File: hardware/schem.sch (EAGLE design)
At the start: 8 parts

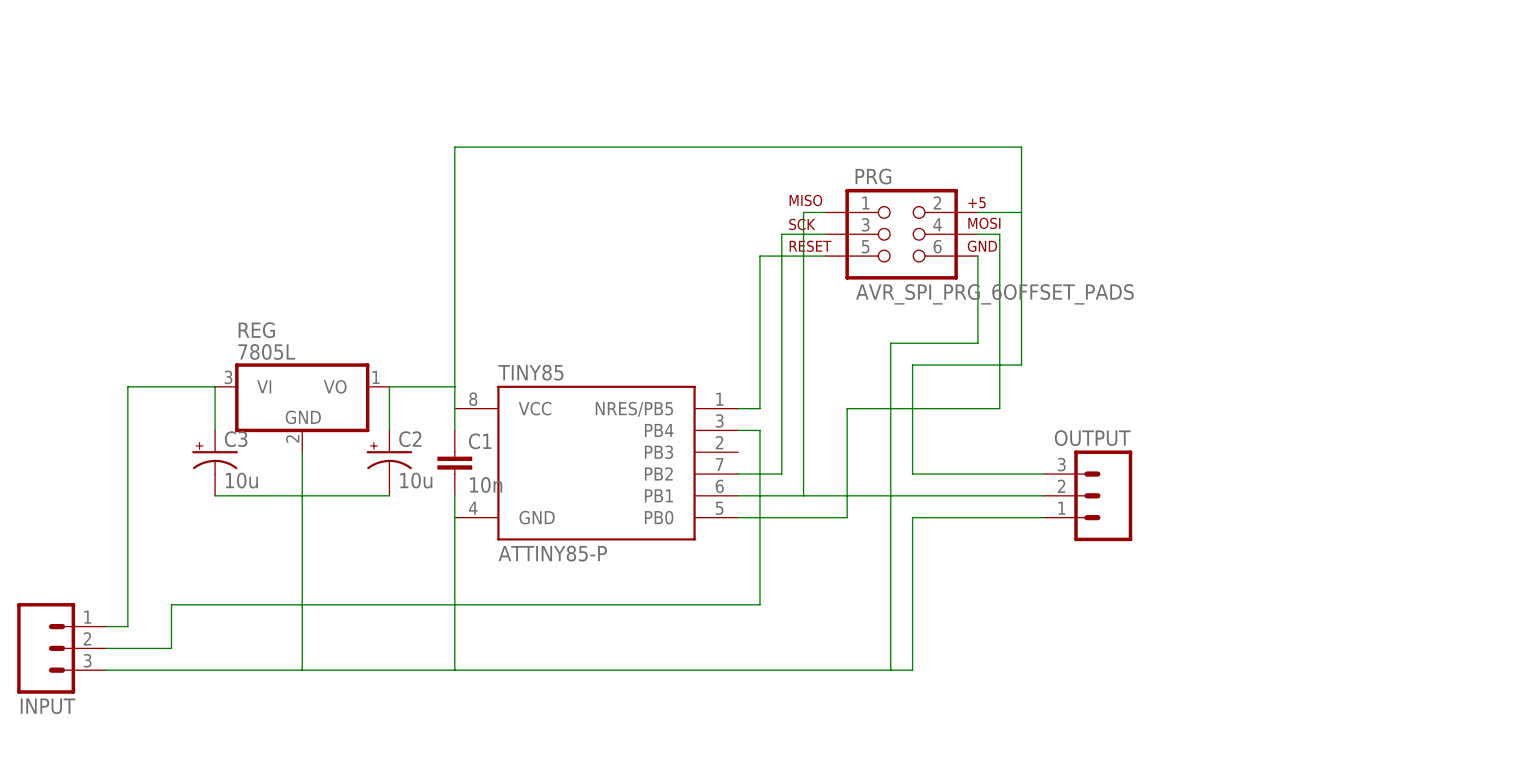
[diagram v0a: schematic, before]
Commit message: Updated Schematic to use integrated H Bridge with DC Motor
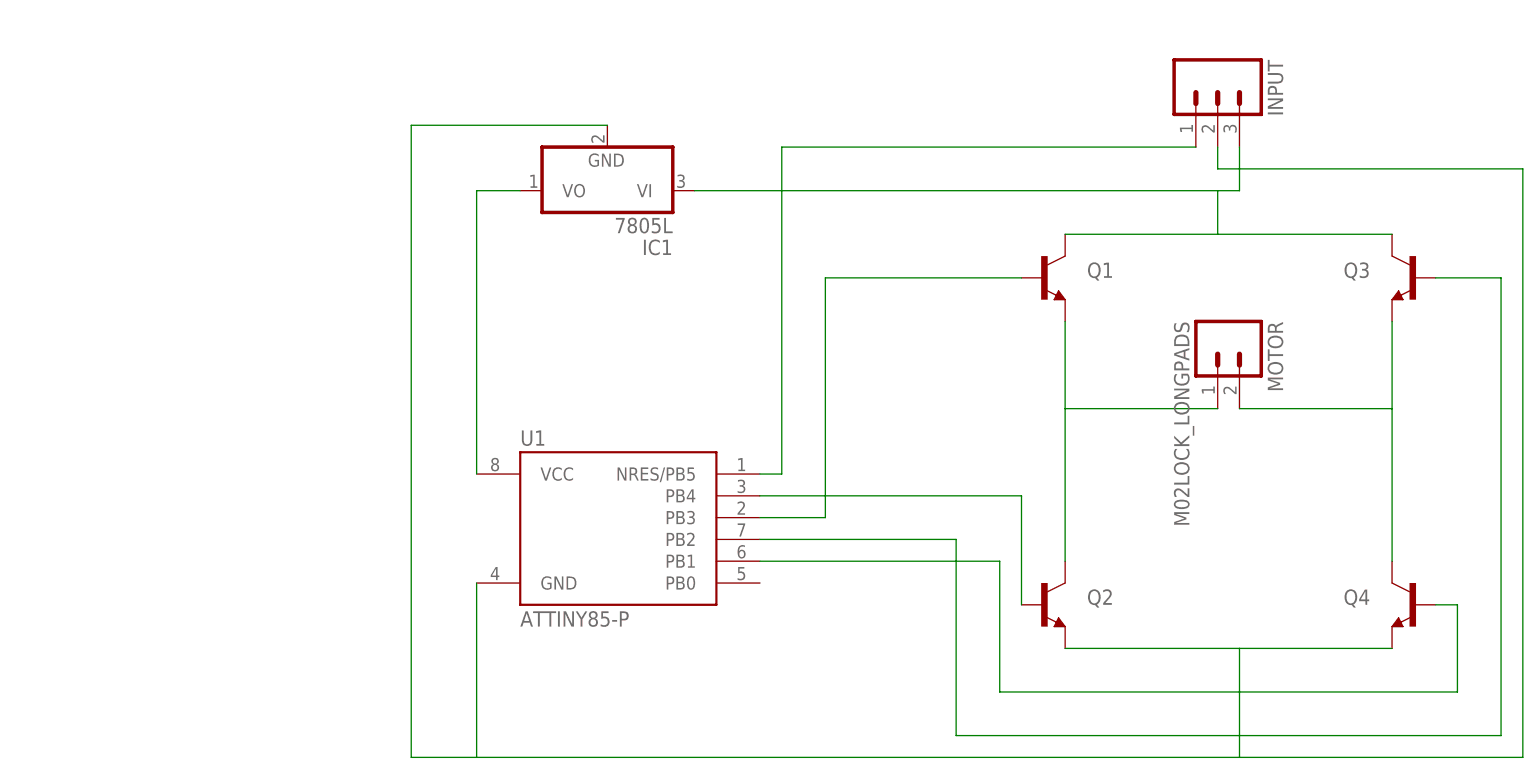
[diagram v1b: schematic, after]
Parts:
- removed C1: 10n, SparkFun-Capacitors:CAPEZ
- removed C2, C3: 10u, rcl:CPOL-USE2.5-6
- removed OUTPUT: (no value), SparkFun-Connectors:M03LOCK_LONGPADS
- removed PRG: AVR_SPI_PRG_6OFFSET_PADS, SparkFun-Connectors:AVR_SPI_PRG_6OFFSET_PADS
- removed REG: 7805L, linear:7805L
- removed TINY85: ATTINY85-P, _hhn_attiny25_45_85:ATTINY85-P
- added IC1: 7805L, linear:7805L
- added MOTOR: M02LOCK_LONGPADS, SparkFun-Connectors:M02LOCK_LONGPADS
- added Q1, Q2, Q3, Q4: (no value), SparkFun-DiscreteSemi:TRANSISTOR_NPNTO-92-AMMO
- added U1: ATTINY85-P, _hhn_attiny25_45_85:ATTINY85-P
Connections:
- new net N$1: MOTOR.1, Q1.E, Q2.C
- new net N$10: IC1.VO, U1.VCC
- net N$2: now also MOTOR.2, Q3.E, Q4.C; no longer PRG.3, TINY85.PB2
- net N$3: now also INPUT.1, U1.NRES/PB5; no longer PRG.5, TINY85.NRES/PB5
- net N$4: now also Q1.B, U1.PB3; no longer PRG.4, TINY85.PB0
- net N$5: now also IC1.VI, INPUT.3, Q1.C, Q3.C; no longer OUTPUT.2, PRG.1, TINY85.PB1
- net N$6: now also IC1.GND, Q2.E, Q4.E, U1.GND; no longer TINY85.PB4
- net N$7: now also Q2.B, U1.PB4; no longer C3.+, INPUT.1, REG.VI
- net N$8: now also Q4.B, U1.PB1; no longer C1.1, C2.+, OUTPUT.3, PRG.2, REG.VO, TINY85.VCC
- net N$9: now also Q3.B, U1.PB2; no longer C1.2, C2.-, C3.-, INPUT.3, OUTPUT.1, PRG.6, REG.GND, TINY85.GND
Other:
- moved on the sheet: INPUT

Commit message: Updated Schematic and Board to include AVR ISP Header
Changed the structure of the H Bridge as well. No longer are you able to independently control all 4 "switches". Now, you control the motor with tow pins (forward or reverse). Layout has yet to bo optimized.
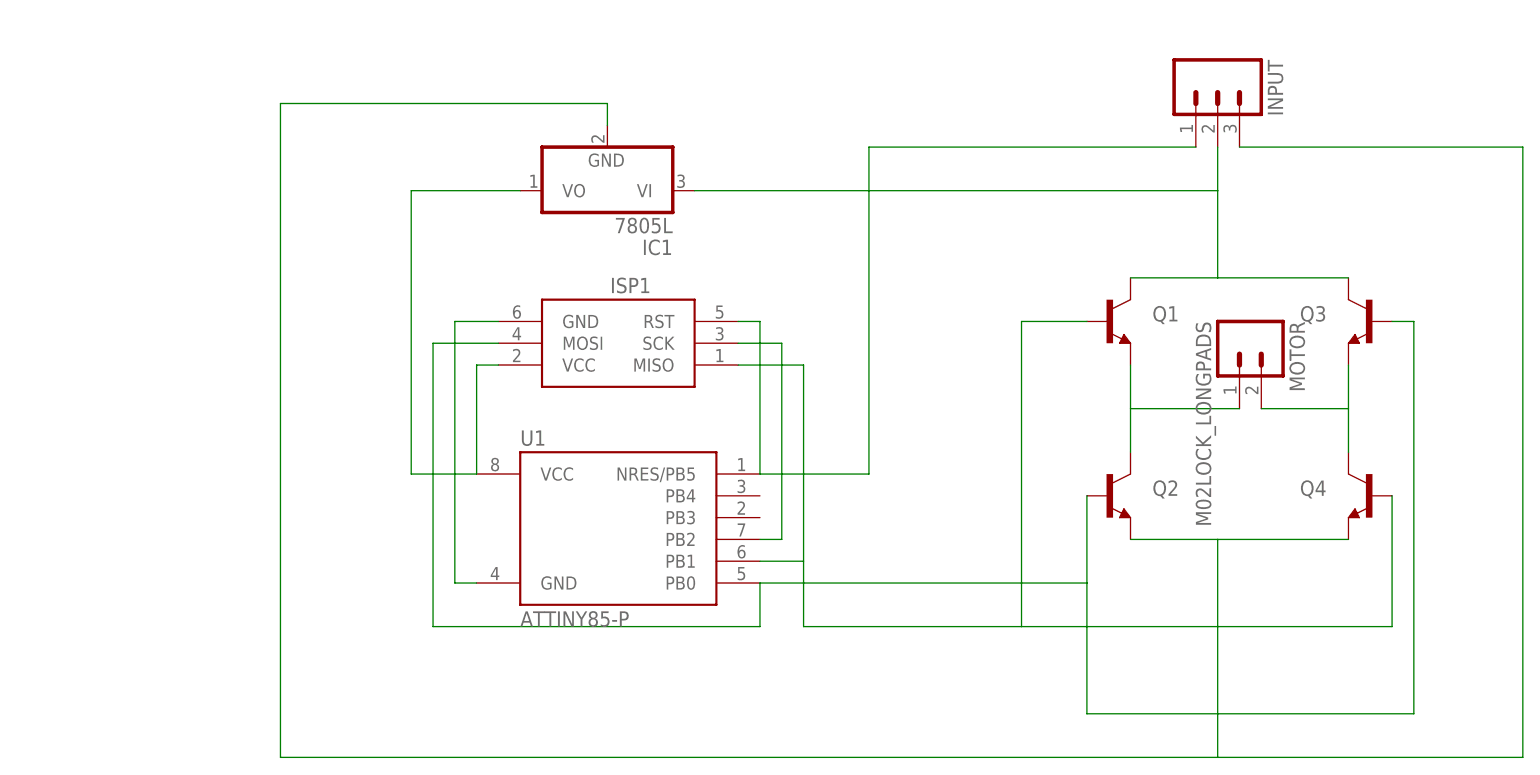
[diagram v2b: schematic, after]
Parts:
- added ISP1: AVRISP-6, adafruit:AVRISP-6
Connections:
- net N$10: now also ISP1.SCK, U1.PB2; no longer IC1.VO, U1.VCC
- net N$3: now also IC1.GND, INPUT.3, Q2.E, Q4.E; no longer INPUT.1, U1.NRES/PB5
- net N$4: now also IC1.VI, INPUT.2, Q1.C, Q3.C; no longer Q1.B, U1.PB3
- net N$5: now also ISP1.MISO, Q1.B, Q4.B, U1.PB1; no longer IC1.VI, INPUT.3, Q1.C, Q3.C
- net N$6: now also ISP1.GND; no longer IC1.GND, INPUT.2, Q2.E, Q4.E
- net N$7: now also IC1.VO, ISP1.VCC, U1.VCC; no longer Q2.B, U1.PB4
- net N$8: now also ISP1.MOSI, Q2.B, Q3.B, U1.PB0; no longer Q4.B, U1.PB1
- net N$9: now also INPUT.1, ISP1.RST, U1.NRES/PB5; no longer Q3.B, U1.PB2
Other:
- moved on the sheet: MOTOR, Q1, Q2, Q3, Q4

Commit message: Cleaned up Schematic and fixed transitors
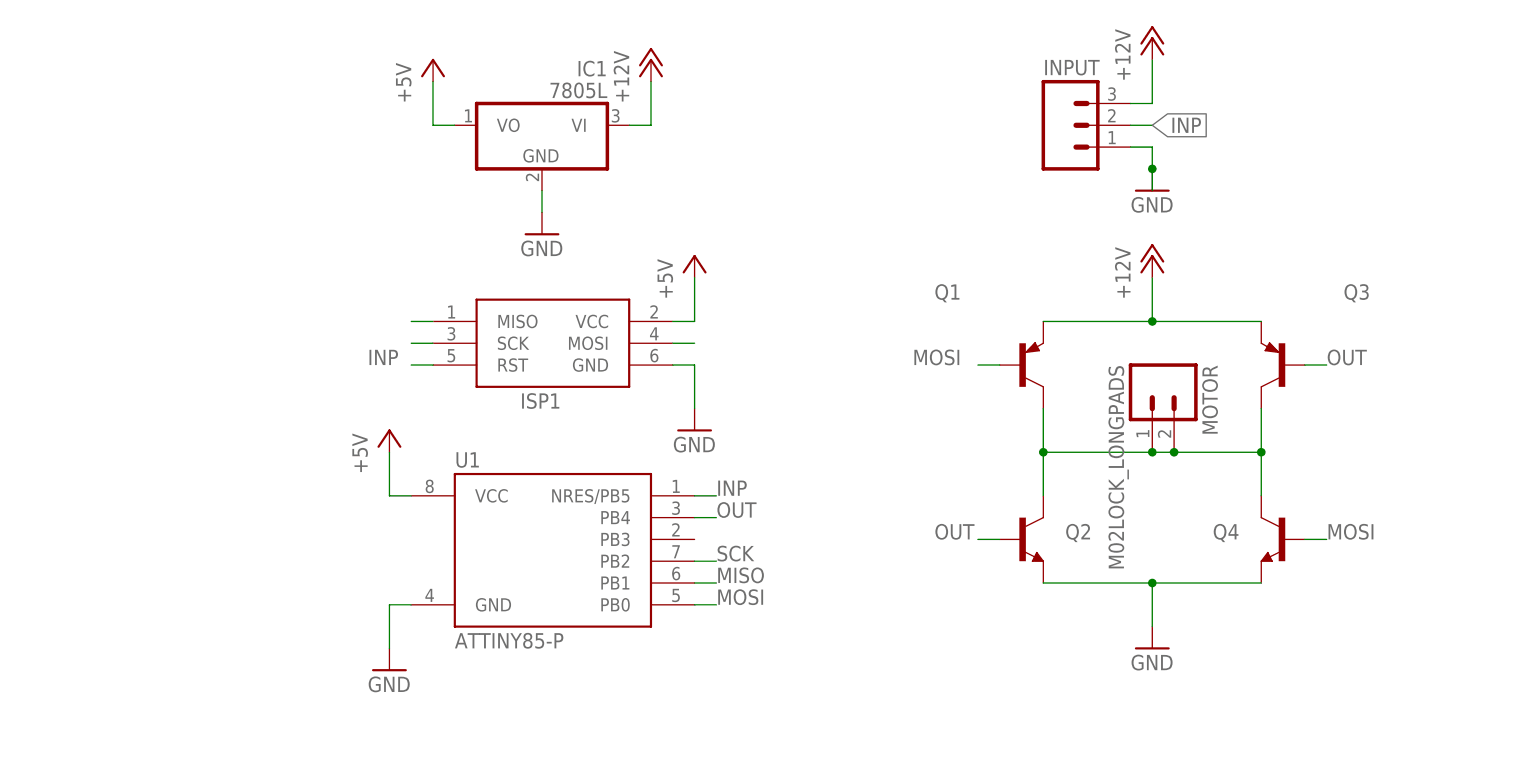
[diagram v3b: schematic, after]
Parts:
- Q1, Q3: device SparkFun-DiscreteSemi:TRANSISTOR_NPNTO-92-AMMO -> transistor:BC448-PNP-TO92-EBC
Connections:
- net N$10 renamed SCK
- net N$7 renamed +5V
- removed net N$2: MOTOR.2, Q3.E, Q4.C
- removed net N$3: IC1.GND, INPUT.3, Q2.E, Q4.E
- removed net N$4: IC1.VI, INPUT.2, Q1.C, Q3.C
- removed net N$5: ISP1.MISO, Q1.B, Q4.B, U1.PB1
- removed net N$6: ISP1.GND, U1.GND
- removed net N$8: ISP1.MOSI, Q2.B, Q3.B, U1.PB0
- removed net N$9: INPUT.1, ISP1.RST, U1.NRES/PB5
- new net +12V: IC1.VI, INPUT.3, Q1.E, Q3.E
- new net GND: IC1.GND, INPUT.1, ISP1.GND, Q2.E, Q4.E, U1.GND
- new net INP: INPUT.2, ISP1.RST, U1.NRES/PB5
- new net MISO: ISP1.MISO, U1.PB1
- new net MOSI: ISP1.MOSI, Q1.B, Q4.B, U1.PB0
- new net OUT: Q2.B, Q3.B, U1.PB4
- net N$1: now also MOTOR.2, Q1.C, Q3.C, Q4.C; no longer Q1.E
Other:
- moved on the sheet: IC1, INPUT, ISP1, MOTOR, Q2, Q4, U1

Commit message: Routed board
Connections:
- new net N$2: MOTOR.2, Q3.C, Q4.C
- net N$1: no longer MOTOR.2, Q3.C, Q4.C
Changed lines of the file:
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@@
 <net name="N$1" class="0">
 <segment>
-<pinref part="Q3" gate="G$1" pin="C"/>
-<pinref part="Q4" gate="G$1" pin="C"/>
-<wire x1="144.78" y1="55.88" x2="144.78" y2="50.8" width="0.1524" layer="91"/>
-<pinref part="MOTOR" gate="G$1" pin="2"/>
-<wire x1="144.78" y1="50.8" x2="144.78" y2="45.72" width="0.1524" layer="91"/>
-<wire x1="144.78" y1="50.8" x2="134.62" y2="50.8" width="0.1524" layer="91"/>
-<junction x="144.78" y="50.8"/>
 <pinref part="MOTOR" gate="G$1" pin="1"/>
-<wire x1="134.62" y1="50.8" x2="132.08" y2="50.8" width="0.1524" layer="91"/>
-<junction x="134.62" y="50.8"/>
 <pinref part="Q1" gate="G$1" pin="C"/>
 <pinref part="Q2" gate="G$1" pin="C"/>
@@
 <wire x1="119.38" y1="50.8" x2="119.38" y2="45.72" width="0.1524" layer="91"/>
 <wire x1="132.08" y1="50.8" x2="119.38" y2="50.8" width="0.1524" layer="91"/>
-<junction x="132.08" y="50.8"/>
 <junction x="119.38" y="50.8"/>
 </segment>
@@
 </segment>
 </net>
+<net name="N$2" class="0">
+<segment>
+<pinref part="MOTOR" gate="G$1" pin="2"/>
+<pinref part="Q4" gate="G$1" pin="C"/>
+<pinref part="Q3" gate="G$1" pin="C"/>
+<wire x1="144.78" y1="55.88" x2="144.78" y2="50.8" width="0.1524" layer="91"/>
+<wire x1="144.78" y1="50.8" x2="144.78" y2="45.72" width="0.1524" layer="91"/>
+<junction x="144.78" y="50.8"/>
+<wire x1="144.78" y1="50.8" x2="134.62" y2="50.8" width="0.1524" layer="91"/>
+</segment>
+</net>

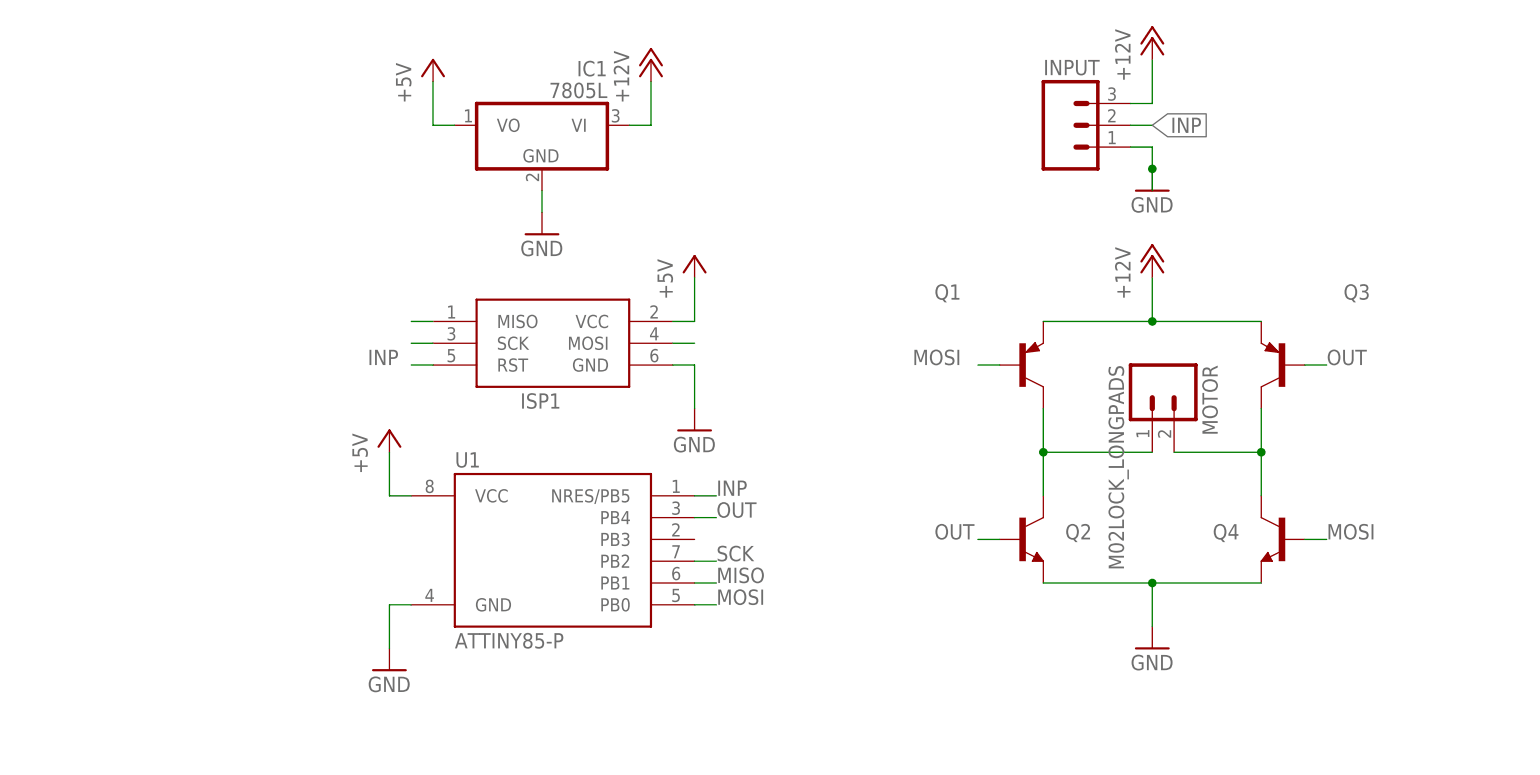
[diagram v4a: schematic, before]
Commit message: selencetd new mosfets and routed
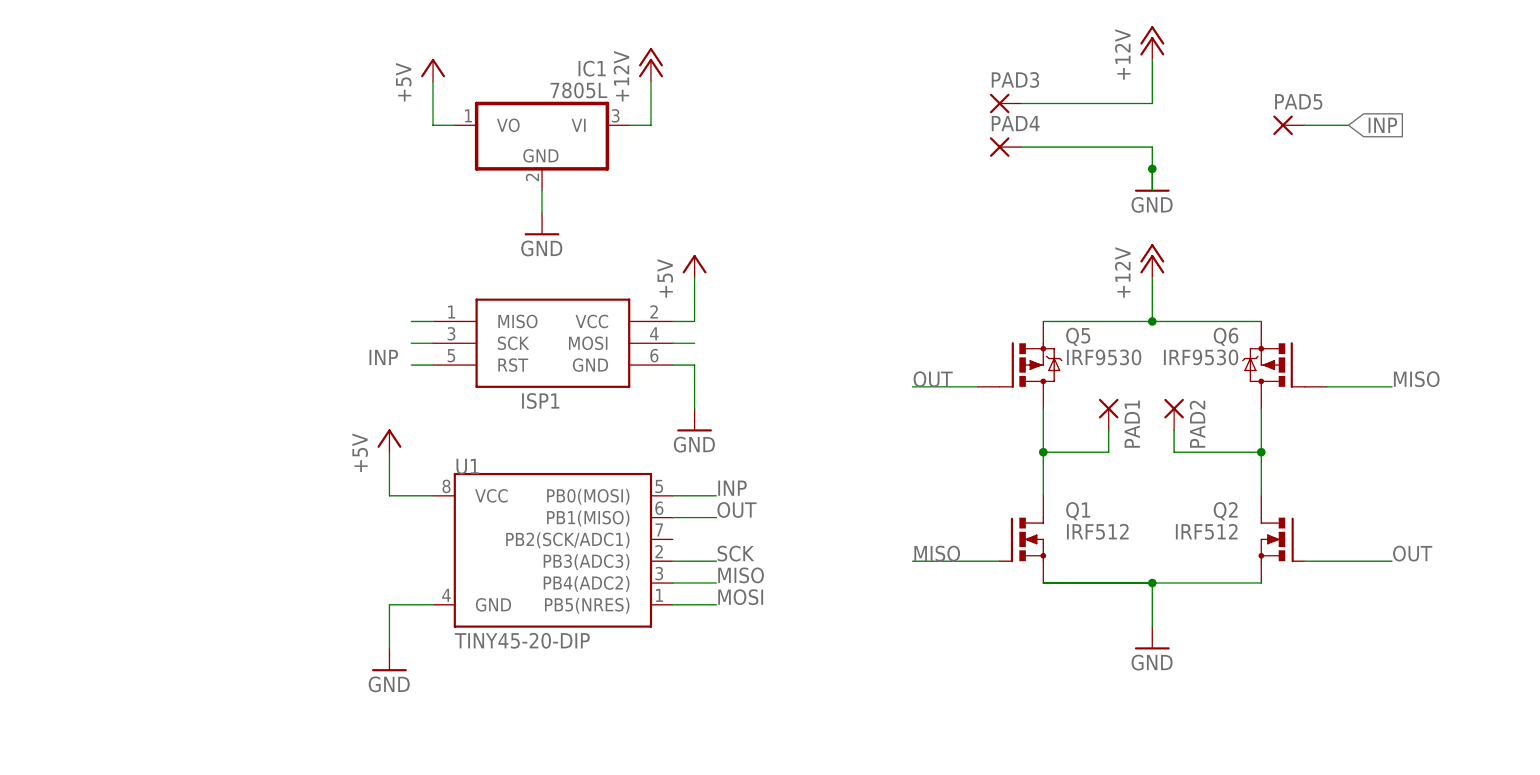
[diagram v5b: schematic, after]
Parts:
- removed INPUT: (no value), SparkFun-Connectors:M03LOCK_LONGPADS
- removed MOTOR: M02LOCK_LONGPADS, SparkFun-Connectors:M02LOCK_LONGPADS
- removed Q3: (no value), transistor:BC448-PNP-TO92-EBC
- removed Q4: (no value), SparkFun-DiscreteSemi:TRANSISTOR_NPNTO-92-AMMO
- added PAD1, PAD2, PAD3, PAD4: (no value), wirepad:3,81/1,3
- added PAD5: (no value), wirepad:2,15/1,0
- added Q5, Q6: IRF9530, transistor-power:IRF9530
- Q1: value (none) -> IRF512; device transistor:BC448-PNP-TO92-EBC -> transistor-power:IRF512
- Q2: value (none) -> IRF512; device SparkFun-DiscreteSemi:TRANSISTOR_NPNTO-92-AMMO -> transistor-power:IRF512
- U1: value ATTINY85-P -> TINY45-20-DIP; device _hhn_attiny25_45_85:ATTINY85-P -> SparkFun-DigitalIC:ATTINY45TINY45-20-DIP
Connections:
- net +12V: now also PAD3.P, Q5.S, Q6.S; no longer INPUT.3, Q1.E, Q3.E
- net GND: now also PAD4.P, Q1.S, Q2.S; no longer INPUT.1, Q2.E, Q4.E
- net INP: now also PAD5.P, U1.PB0(MOSI); no longer INPUT.2, U1.NRES/PB5
- net MISO: now also Q1.G, Q6.G, U1.PB4(ADC2); no longer U1.PB1
- net MOSI: now also U1.PB5(NRES); no longer Q1.B, Q4.B, U1.PB0
- net N$1: now also PAD1.P, Q1.D, Q5.D; no longer MOTOR.1, Q1.C, Q2.C
- net N$2: now also PAD2.P, Q2.D, Q6.D; no longer MOTOR.2, Q3.C, Q4.C
- net OUT: now also Q2.G, Q5.G, U1.PB1(MISO); no longer Q2.B, Q3.B, U1.PB4
- net SCK: now also U1.PB3(ADC3); no longer U1.PB2
